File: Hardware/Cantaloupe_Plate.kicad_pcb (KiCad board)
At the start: 2 copper layers, 142.1 x 117 mm, 36 parts, among them SW1 MX, SW10 MX, SW11 MX, SW12 MX, SW13 MX, SW14 MX, SW15 MX, SW16 MX, SW17 MX, SW18 MX, SW19 MX, SW2 MX, SW20 MX, SW21 MX, SW22 MX, SW23 MX, SW24 MX, SW25 MX, SW26 MX, SW27 MX, SW28 MX, SW29 MX, SW3 MX, SW30 MX, SW31 MX, SW4 MX, SW5 MX, SW6 MX, SW7 MX, SW8 MX, SW9 MX

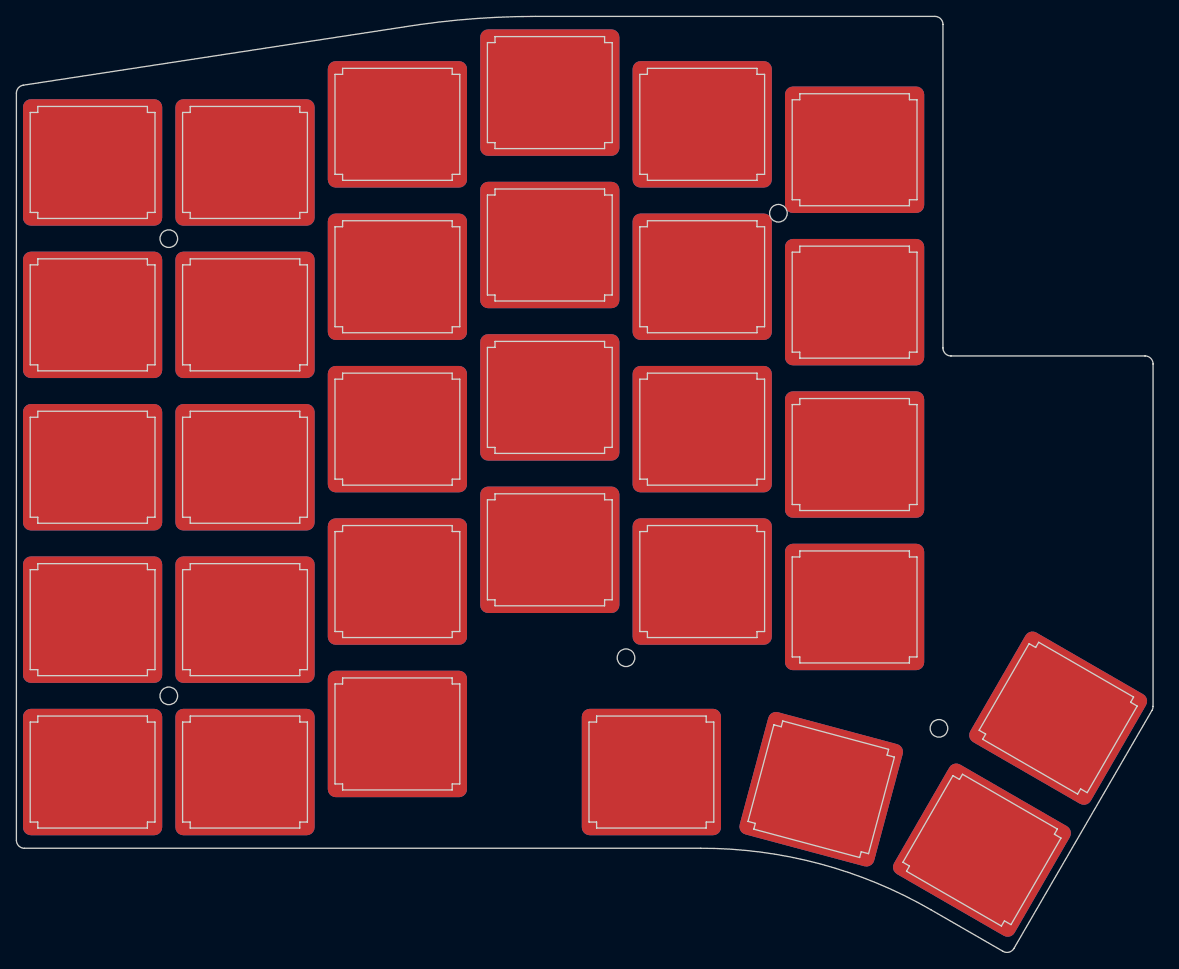
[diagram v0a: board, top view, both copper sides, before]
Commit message: Updated to V1.3.
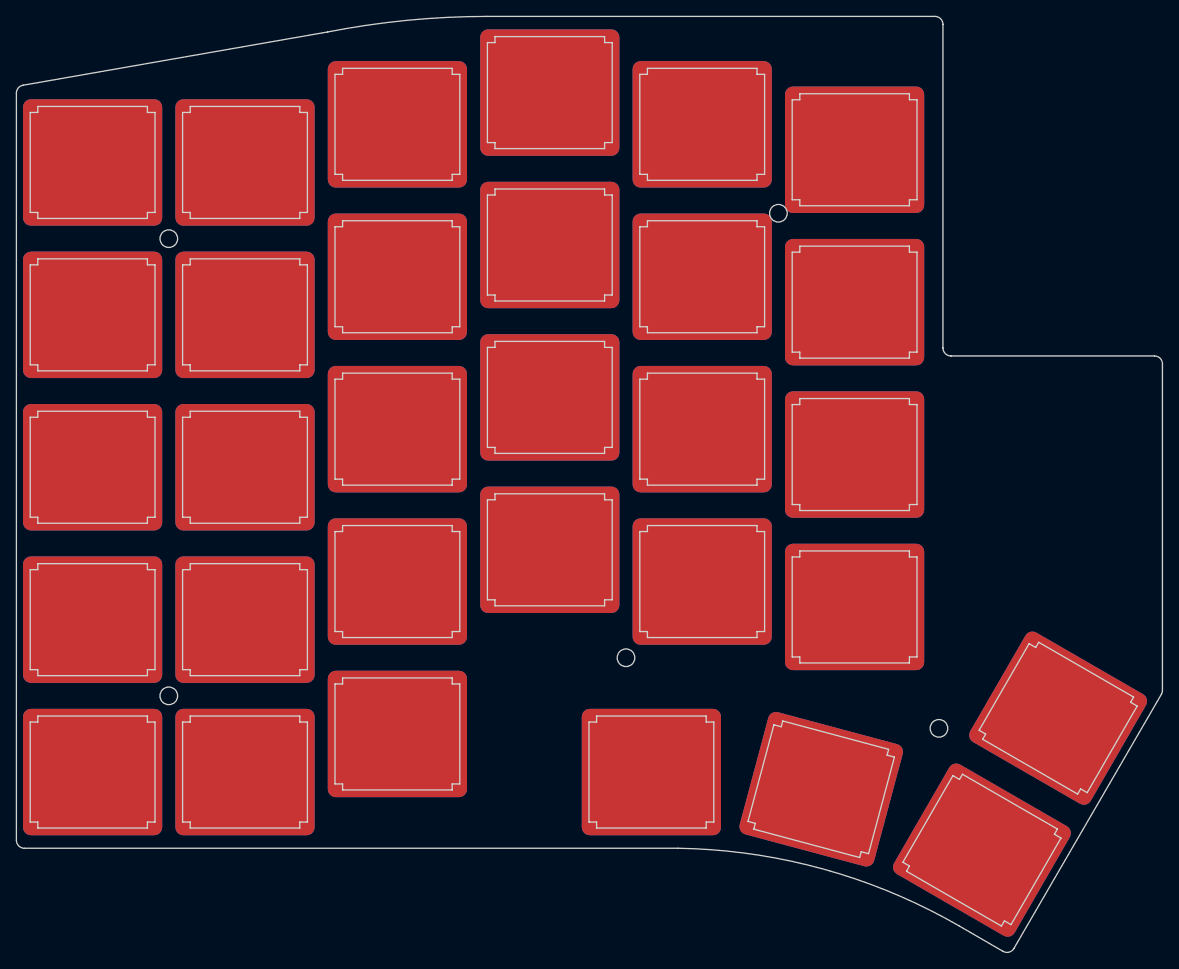
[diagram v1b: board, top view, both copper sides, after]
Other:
- board size 142.1 x 117 mm -> 143.3 x 117 mm

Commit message: Changed OLED support to 0.96" OLED
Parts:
- added SW35: Reset, MountingHole:MountingHole_3.5mm, F.Cu at (324.3, 100.3)
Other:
- outline, holes or cut-outs redrawn

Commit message: Changed orientation of 1u switches in thumb cluster. Updated plate to add 2u support.
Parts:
- removed the REF** at (310.6, 121.5)
- removed the REF** at (271.5, 112.7)
- removed the REF** at (290.5, 57.1)
- removed the REF** at (214.3, 117.5)
- removed the REF** at (214.3, 60.3)
- removed SW10, SW30, SW31, SW5: MX, Keebio-Parts:MX-Alps_Switch_Cutout
- added REF**: MX-Alps_Switch_Cutout, Keebio-Parts:MX-Alps_Switch_Cutout-1u_2u, F.Cu at (138.5, 109.2)
- added REF**: MX-Alps_Switch_Cutout, Keebio-Parts:MX-Alps_Switch_Cutout-1u_2u, F.Cu at (32.1, 107.7)
- added REF**: MountingHole_2.2mm_M2, MountingHole:MountingHole_2.2mm_M2, F.Cu at (128.4, 102.2)
- added REF**: MountingHole_2.2mm_M2, MountingHole:MountingHole_2.2mm_M2, F.Cu at (89.2, 93.4)
- added REF**: MountingHole_2.2mm_M2, MountingHole:MountingHole_2.2mm_M2, F.Cu at (108.3, 37.8)
- added REF**: MountingHole_2.2mm_M2, MountingHole:MountingHole_2.2mm_M2, F.Cu at (32.1, 98.2)
- added REF**: MountingHole_2.2mm_M2, MountingHole:MountingHole_2.2mm_M2, F.Cu at (32.1, 41.0)
- moved SW22 183.2 mm to (98.8, 64.8)
- moved SW3 183.2 mm to (22.6, 69.6)
- moved SW4 183.2 mm to (22.6, 88.6)
- moved SW19 183.2 mm to (79.7, 79.9)
- moved SW25 183.2 mm to (117.8, 29.9)
- moved SW26 183.2 mm to (117.8, 49.0)
- moved SW27 183.2 mm to (117.8, 68.0)
- moved SW28 183.2 mm to (117.8, 87.1)
- moved SW11 183.2 mm to (60.7, 26.7)
- moved SW12 183.2 mm to (60.7, 45.8)
- moved SW14 183.2 mm to (60.7, 83.9)
- moved SW15 183.2 mm to (60.7, 102.9)
- moved SW16 183.2 mm to (79.7, 22.8)
- moved SW17 183.2 mm to (79.7, 41.8)
- moved SW18 183.2 mm to (79.7, 60.9)
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
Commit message: Added proper OLED support.
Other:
- outline, holes or cut-outs redrawn
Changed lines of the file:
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@@
     (solder_mask_min_width 0.25)
     (aux_axis_origin 0 0)
+    (grid_origin 154.151249 73.06495)
     (visible_elements 7FFFF7FF)
     (pcbplotparams
@@
     (pad 1 np_thru_hole circle (at 0 0) (size 2.2 2.2) (drill 2.2) (layers *.Cu *.Mask))
   )
-  (gr_line (start 153.691247 53.614951) (end 131.441248 53.614951) (layer Edge.Cuts) (width 0.1))
-  (gr_line (start 153.691247 65.014951) (end 153.691247 53.614951) (layer Edge.Cuts) (width 0.1))
-  (gr_line (start 131.441247 65.014951) (end 153.691247 65.014951) (layer Edge.Cuts) (width 0.1))
-  (gr_line (start 131.441248 53.614951) (end 131.441247 65.014951) (layer Edge.Cuts) (width 0.1))
+  (gr_line (start 156.292246 75.31495) (end 156.29225 97.486217) (layer Edge.Cuts) (width 0.1))
+  (gr_line (start 128.651249 75.31495) (end 156.292246 75.31495) (layer Edge.Cuts) (width 0.1))
+  (gr_line (start 128.651249 47.56495) (end 128.651249 75.31495) (layer Edge.Cuts) (width 0.1))
+  (gr_line (start 156.292246 47.56495) (end 128.651249 47.56495) (layer Edge.Cuts) (width 0.1))
   (gr_arc (start 155.292242 14.243702) (end 155.292243 13.243698) (angle 90) (layer Edge.Cuts) (width 0.1))
   (gr_line (start 71.962558 13.243701) (end 155.292243 13.243698) (layer Edge.Cuts) (width 0.1))
-  (gr_line (start 156.292246 14.243703) (end 156.292246 97.486216) (layer Edge.Cuts) (width 0.1))
+  (gr_line (start 156.292246 14.243703) (end 156.292246 47.56495) (layer Edge.Cuts) (width 0.1))
   (gr_line (start 13.885224 21.845295) (end 51.939286 15.190412) (layer Edge.Cuts) (width 0.1))
   (gr_arc (start 71.962559 117.1937) (end 71.962558 13.243701) (angle -11.10596181) (layer Edge.Cuts) (width 0.1))

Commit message: Updated to V1.4.
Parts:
- moved SW35 24.1 mm to (142.1, 56.9)
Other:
- outline, holes or cut-outs redrawn

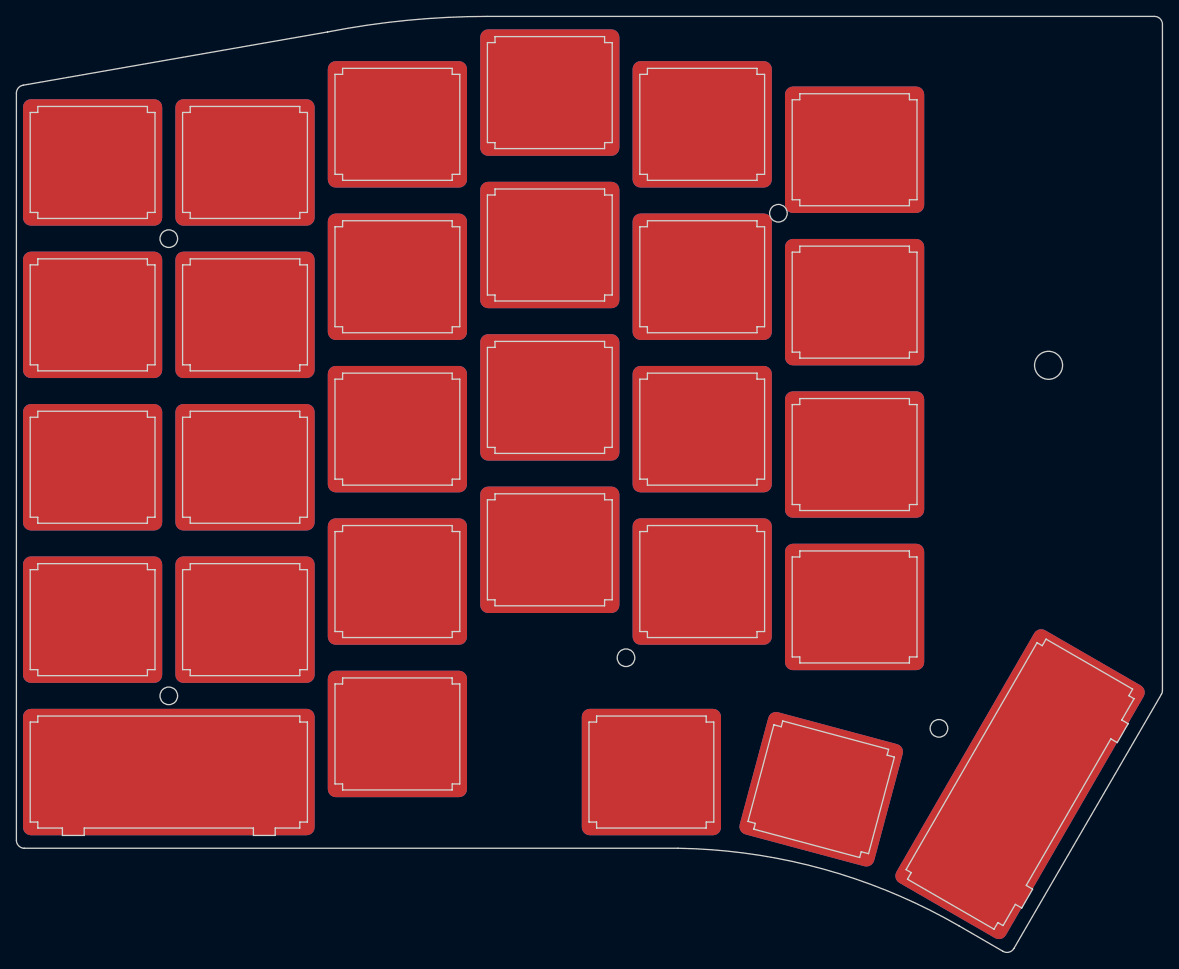
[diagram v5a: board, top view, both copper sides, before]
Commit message: Added SMK support
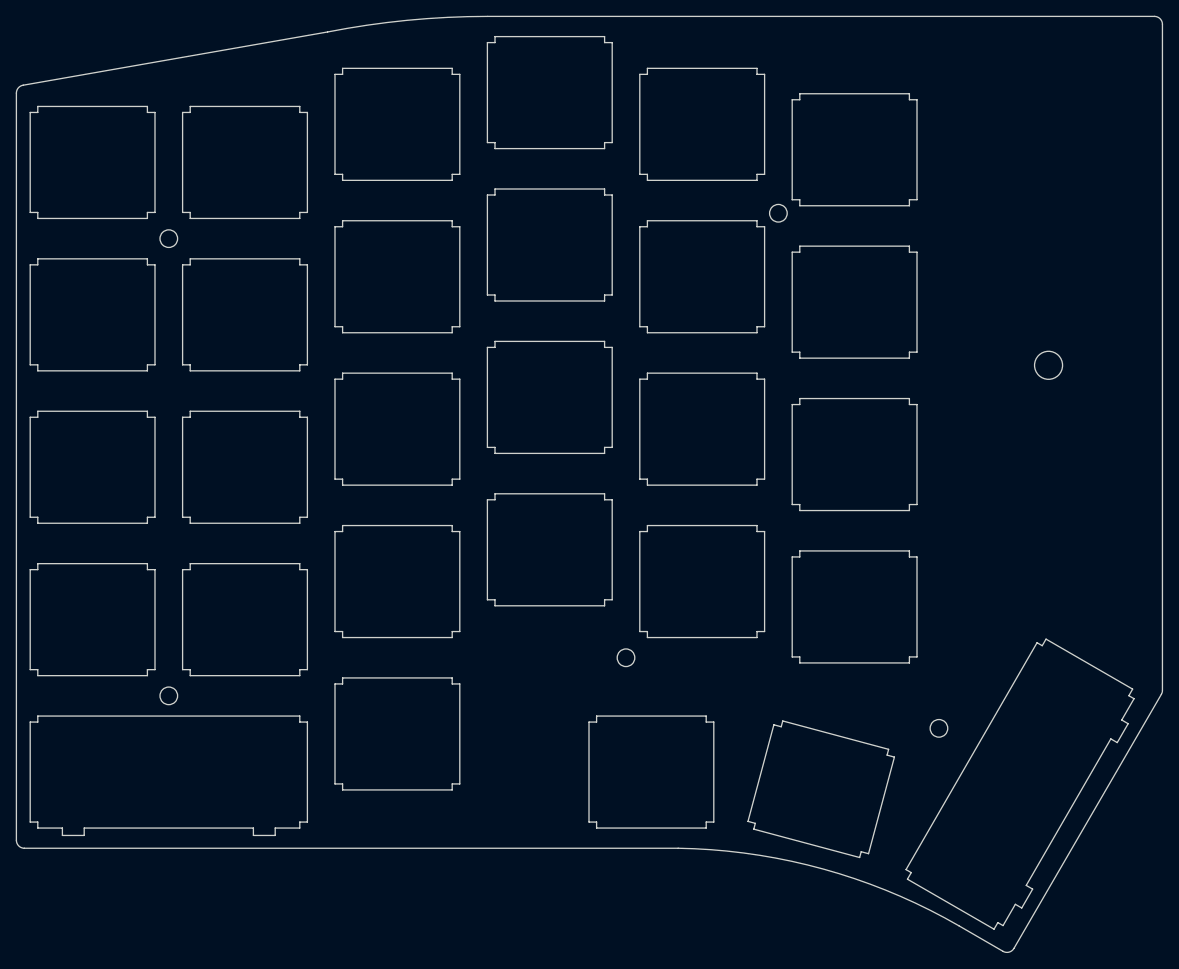
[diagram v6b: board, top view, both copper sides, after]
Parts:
- REF** (x2): footprint Keebio-Parts:MX-Alps_Switch_Cutout-1u_2u -> Cantaloupe:MX-Alps_Switch_Cutout-1u_2u
- SW1, SW11, SW12, SW13, SW14, SW15, SW16, SW17, SW18, SW19, SW2, SW20, SW21, SW22, SW23, SW24, SW25, SW26, SW27, SW28, SW29, SW3, SW4, SW6, SW7, SW8, SW9: footprint Keebio-Parts:MX-Alps_Switch_Cutout -> Cantaloupe:MX-Alps_Switch_Cutout
